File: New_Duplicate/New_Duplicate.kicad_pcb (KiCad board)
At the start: 4 copper layers, 100 x 100 mm, 243 parts, among them J1 VBAT, J10 CLK_2, J11 I_LO, J12 Q_LO, J13 I_0, J14 I_180, J15 Q_90, J16 Q_270, J17 I_RAW, J18 Conn_01x02_Female, J19 Conn_01x02_Female, J2 GND, J20 Q_RAW, J21 SDR Out, J23 VDDA, J24 CLK_0, J25 OLED, J26 +5V, J3 3.3VA, J33 XFIL_IN, J34 XFIL_OUT, J35 3.5mm_Jack, J36 +5RAW, J37 4.5V, J38 DAC_FLT, J39 VDD, J4 4.5VA, J40 DAC_FMT, J41 V_DIV, J42 VDDA/2, J45 CENTER_TAP, J46 3.5mm_Jack, J47 FIL_IN, J5 Conn_Coaxial, J6 Conn_01x02, J7 Micro_SD-TF_PUSH, J8 FIL_OUT, J9 CLK_1, SW1 RotaryEncoder_Switch_MP, SW6 09.03290.01, T1 Transformer_1P_SS, U1 TPS7A2045PDQN, U10 OPA1612AID, U11 INA821ID, U12 PCM1808PWR, U13 SN74CBT3253CDBR, U14 PCM5102A, U2 TPS7A2045PDQN, U3 TPS72733DSER, U4 Pico, U5 Si5351A-B-GT, U6 SN74AC74DR, U8 SN74CBT3253CDBR, U9 INA821ID, Y1 ASTX-H11-24.576MHZ-T

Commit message: More tracing done. Not completly finished.
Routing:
- net /ADC-24bit/VDDA/2: track 90.9 -> 30.8 mm
- net Net-(J46-PadR): track 0.00 -> 58.4 mm
- net /BCK: track 0.00 -> 44.8 mm
- net GND: track 59.4 -> 98.2 mm
- net /SDIN: track 0.00 -> 33.2 mm
- net /Raspberry_Pi_Pico/GPIO12: track 0.00 -> 27.1 mm
- net /Raspberry_Pi_Pico/GPIO13: track 0.00 -> 26.9 mm
- net Net-(U14-OUTR): track 0.00 -> 24.6 mm
- net /SCL: track 0.00 -> 20.5 mm
- net /LRCK: track 0.00 -> 20.1 mm
- net Net-(C59-Pad2): track 0.00 -> 20.1 mm
- net /SDA: track 0.00 -> 19.2 mm
- net /Raspberry_Pi_Pico/RST: track 0.00 -> 14.2 mm
- net Net-(U14-AVDD): track 0.00 -> 12.4 mm
- net Net-(e5-B): track 0.00 -> 9.75 mm
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
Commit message: More Tracing
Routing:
- net /ADC-24bit/VDDA/2: track 30.8 -> 83.0 mm
- net GND: track 98.2 -> 126.5 mm
- net +3.3V: track 7.81 -> 32.3 mm
- net +3.3VA: track 6.90 -> 16.6 mm

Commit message: small wire connections
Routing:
- net GND: track 126.5 -> 137.9 mm
- net /Raspberry_Pi_Pico/VSYS: track 0.00 -> 11.4 mm, vias 0 -> 1
- net +5V: track 0.00 -> 2.79 mm
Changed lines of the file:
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@@
+	)
+	(segment
+		(start 157.895 83.412679)
+		(end 158.412679 83.412679)
+		(width 0.2)
+		(layer "F.Cu")
+		(net "GND")
 	)
 	(segment
@@
 	)
 	(segment
+		(start 156.205 83.412679)
+		(end 155.895 83.722679)
+		(width 0.2)
+		(layer "F.Cu")
+		(net "GND")
+	)
+	(segment
 		(start 140.58 79.252679)
 		(end 138.729574 79.252679)
@@
 	)
 	(segment
+		(start 158.412679 83.412679)
+		(end 158.772679 83.772679)
+		(width 0.2)
+		(layer "F.Cu")
+		(net "GND")
+	)
+	(segment
 		(start 134.020001 108.497538)
 		(end 133.545715 108.497538)
@@
 	)
 	(segment
+		(start 157.895 83.412679)
+		(end 156.205 83.412679)
+		(width 0.2)
+		(layer "F.Cu")
+		(net "GND")
+	)
+	(segment
 		(start 116.665 90.072679)
 		(end 116.665 92.202423)
@@
 	)
 	(segment
+		(start 157.895 83.412679)
+		(end 157.895 82.605)
+		(width 0.2)
+		(layer "F.Cu")
+		(net "GND")
+	)
+	(segment
 		(start 128.912257 108.223824)
 		(end 128.912257 106.485282)
@@
 	)
 	(segment
+		(start 157.605 82.315)
+		(end 157.605 78.552679)
+		(width 0.2)
+		(layer "F.Cu")
+		(net "GND")
+	)
+	(segment
 		(start 130.352257 113.523824)
 		(end 130.552257 113.723824)
@@
 	)
 	(segment
+		(start 158.772679 83.772679)
+		(end 162.025 83.772679)
+		(width 0.2)
+		(layer "F.Cu")
+		(net "GND")
+	)
+	(segment
 		(start 121.975 94.652679)
 		(end 121.975 92.552679)
@@
 		(start 141.4 124.69)
 		(end 141.57 124.52)
+		(width 0.2)
+		(layer "F.Cu")
+		(net "GND")
+	)
+	(segment
+		(start 157.895 82.605)
+		(end 157.605 82.315)
 		(width 0.2)
 		(layer "F.Cu")
@@
 	)
 	(segment
+		(start 161.505 68.852679)
+		(end 161.505 71.612679)
+		(width 0.2)
+		(layer "B.Cu")
+		(net "+5V")
+	)
+	(segment
+		(start 161.505 71.612679)
+		(end 161.485 71.632679)
+		(width 0.2)
+		(layer "B.Cu")
+		(net "+5V")
+	)
+	(segment
 		(start 104.157423 52.277471)
 		(end 107 50)
@@
 	)
 	(segment
+		(start 157.605 72.972679)
+		(end 158.945 71.632679)
+		(width 0.2)
+		(layer "F.Cu")
+		(net "/Raspberry_Pi_Pico/VSYS")
+	)
+	(segment
+		(start 159.105 77.752679)
+		(end 157.805 77.752679)
+		(width 0.2)
+		(layer "F.Cu")
+		(net "/Raspberry_Pi_Pico/VSYS")
+	)
+	(segment
+		(start 157.605 77.552679)
+		(end 157.605 72.972679)
+		(width 0.2)
+		(layer "F.Cu")
+		(net "/Raspberry_Pi_Pico/VSYS")
+	)
+	(segment
+		(start 157.805 77.752679)
+		(end 157.605 77.552679)
+		(width 0.2)
+		(layer "F.Cu")
+		(net "/Raspberry_Pi_Pico/VSYS")
+	)
+	(via
+		(at 160.205 68.852679)
+		(size 0.6)
+		(drill 0.3)
+		(layers "F.Cu" "B.Cu")
+		(net "/Raspberry_Pi_Pico/VSYS")
+	)
+	(segment
+		(start 158.945 71.632679)
+		(end 160.205 70.372679)
+		(width 0.2)
+		(layer "B.Cu")
+		(net "/Raspberry_Pi_Pico/VSYS")
+	)
+	(segment
+		(start 160.205 70.372679)
+		(end 160.205 68.852679)
+		(width 0.2)
+		(layer "B.Cu")
+		(net "/Raspberry_Pi_Pico/VSYS")
+	)
+	(segment

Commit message: trace...
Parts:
- moved J45 0.52 mm to (108.4, 122.5)
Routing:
- net /I: track 11.7 -> 44.9 mm
- net /Q: track 14.8 -> 43.9 mm
- net /ADC-24bit/VDDA/2: track 83.0 -> 92.3 mm
- net Net-(C97-Pad1): track 0.00 -> 4.71 mm
- net GND: track 137.9 -> 142.6 mm

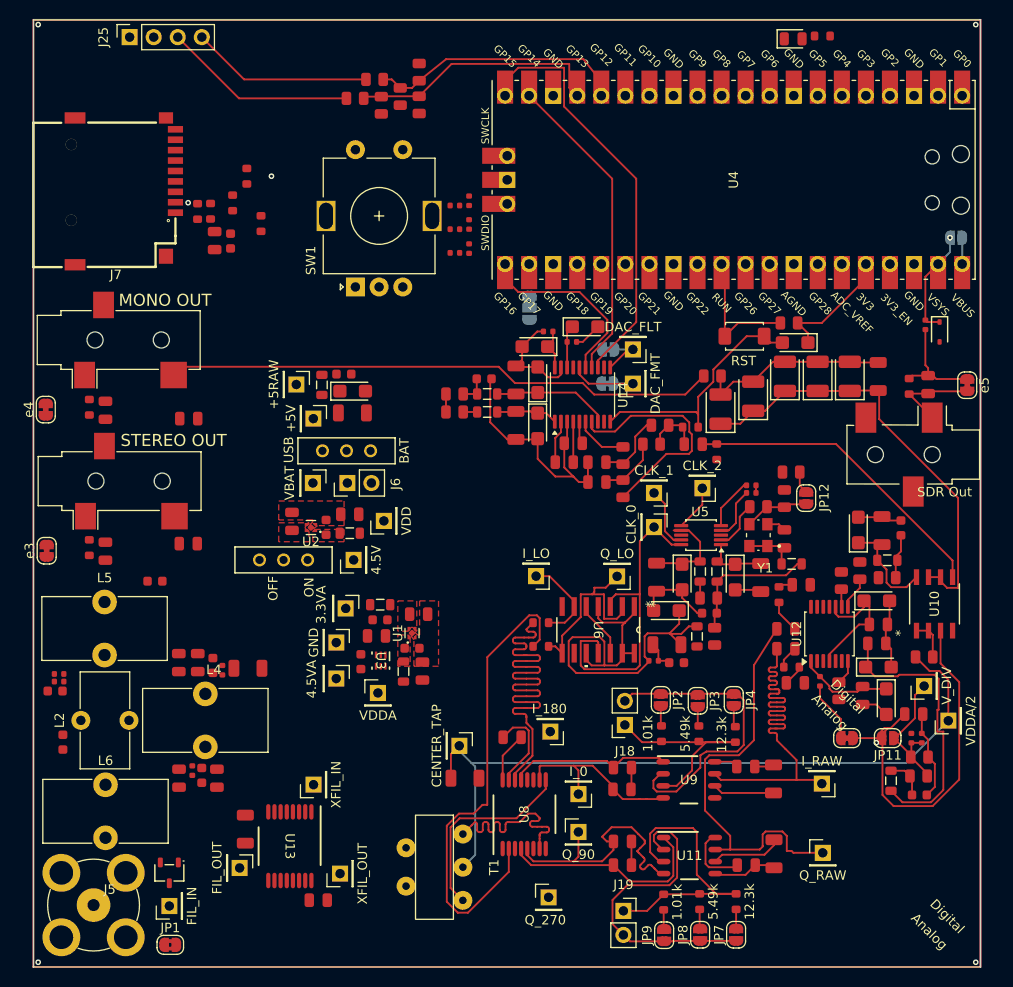
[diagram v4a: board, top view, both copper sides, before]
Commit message: trace to trace
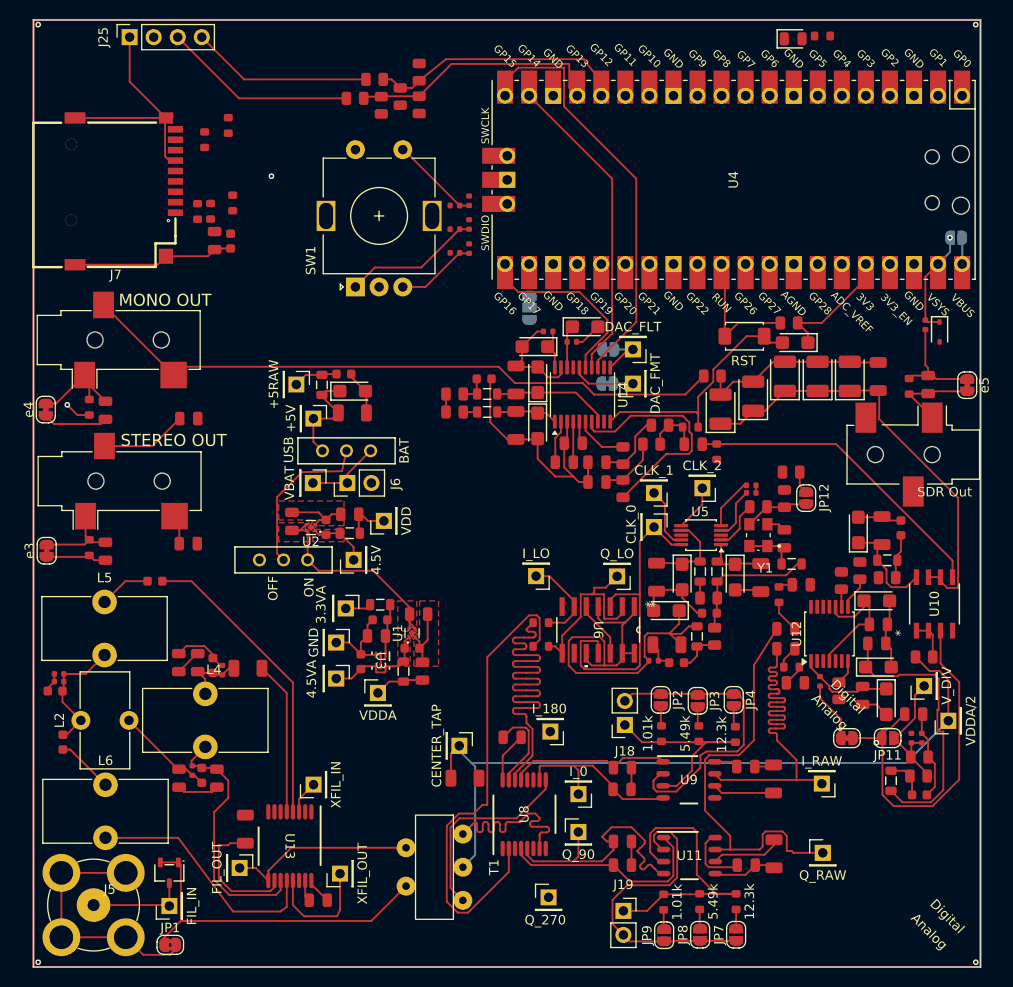
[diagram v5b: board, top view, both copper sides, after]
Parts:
- moved R54 10.9 mm to (84.0, 57.0), turned to 90 degrees
- moved R50 5.89 mm to (81.5, 58.5), turned to -90 degrees
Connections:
- FB19 pad 1: +3.3VA -> GND
- J3 pad 1: +3.3VA -> GND
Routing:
- net GND: track 142.6 -> 229.6 mm, vias 0 -> 1
- net GNDA: track 0.00 -> 55.2 mm
- net Net-(U13-1B3): track 0.00 -> 31.9 mm
- net Net-(J5-Ext): track 0.00 -> 27.2 mm
- net Net-(U13-2B2): track 0.00 -> 27.1 mm
- net Net-(U13-2B3): track 0.00 -> 26.0 mm
- net Net-(U1-EN): track 0.00 -> 23.4 mm
- net /Antenna/Signal_OUT: track 0.00 -> 20.2 mm
- net Net-(ON/OFF1-Pad1): track 0.00 -> 17.1 mm
- net Net-(U13-1B2): track 0.00 -> 16.2 mm
- net /ANG_A: track 0.00 -> 14.5 mm
- net Net-(U13-2B1): track 0.00 -> 13.7 mm
- net Net-(C2-Pad1): track 0.00 -> 13.4 mm
- net Net-(J34-Pin_1): track 0.00 -> 12.3 mm
- net Net-(e4-B): track 0.00 -> 11.8 mm
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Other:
- board text added: "Rotary encoder could be moved down and wires nicely The SD card wires/capacitors need to be fixed. DAC SDIN and BCK need to be rewired somehow. VIAS? Stereo & Mono OUT need to be wired to DAC. long wires and they cross so we have to restructure?"

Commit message: back copper tracing for raspberry pi done
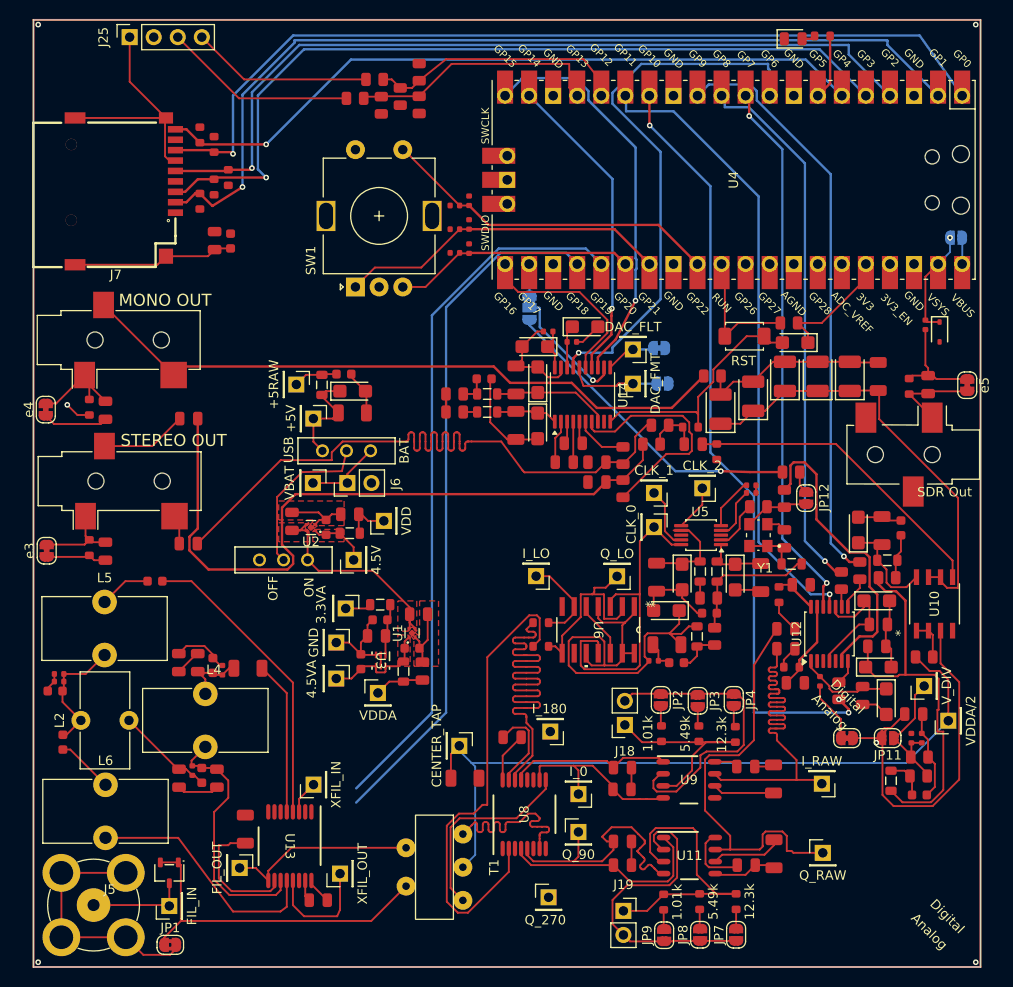
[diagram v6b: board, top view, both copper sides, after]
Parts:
- moved JP10 5.82 mm to (129.8, 84.3), turned to 0 degrees
- moved JP6 5.38 mm to (129.5, 80.5), turned to 180 degrees
- moved R54 3.16 mm to (81.0, 58.0)
- moved R47 2.72 mm to (84.0, 62.5)
- moved R49 2.58 mm to (82.5, 63.5)
- moved R50 1.12 mm to (82.5, 59.0)
- moved R51 1.10 mm to (81.0, 65.0)
- moved C29 0.31 mm to (152.5, 112.0)
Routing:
- net /CS: track 0.00 -> 97.1 mm, vias 0 -> 1
- net /MISO: track 0.00 -> 95.3 mm, vias 0 -> 1
- net /SPI_CK: track 0.00 -> 88.5 mm, vias 0 -> 1
- net /MOSI: track 0.00 -> 87.5 mm, vias 0 -> 1
- net /WS: track 0.00 -> 81.5 mm, vias 0 -> 3
- net /SD_CD: track 0.00 -> 76.3 mm, vias 0 -> 1
- net /CTL1: track 0.00 -> 74.7 mm
- net /CTL2: track 0.00 -> 73.0 mm
- net Net-(C42-Pad1): track 6.55 -> 74.6 mm
- net /MD1: track 0.00 -> 67.1 mm, vias 0 -> 1
- net Net-(C43-Pad1): track 7.54 -> 74.4 mm
- net /BCKO: track 0.00 -> 62.0 mm, vias 0 -> 1
- net /MUTE: track 0.00 -> 58.4 mm, vias 0 -> 1
- net /FMT: track 0.00 -> 57.7 mm, vias 0 -> 2
- net /DATA: track 0.00 -> 57.5 mm, vias 0 -> 1
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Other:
- board text added: "V_DIV needs a connection NOT set"
